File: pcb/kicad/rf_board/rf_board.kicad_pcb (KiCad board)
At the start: 2 copper layers, 89.5 x 70 mm, 14 parts, among them J1 B2B_A, J2 B2B_B, J3 UART_DBG, U1 CC1101_433_MODULE, U2 HC-05

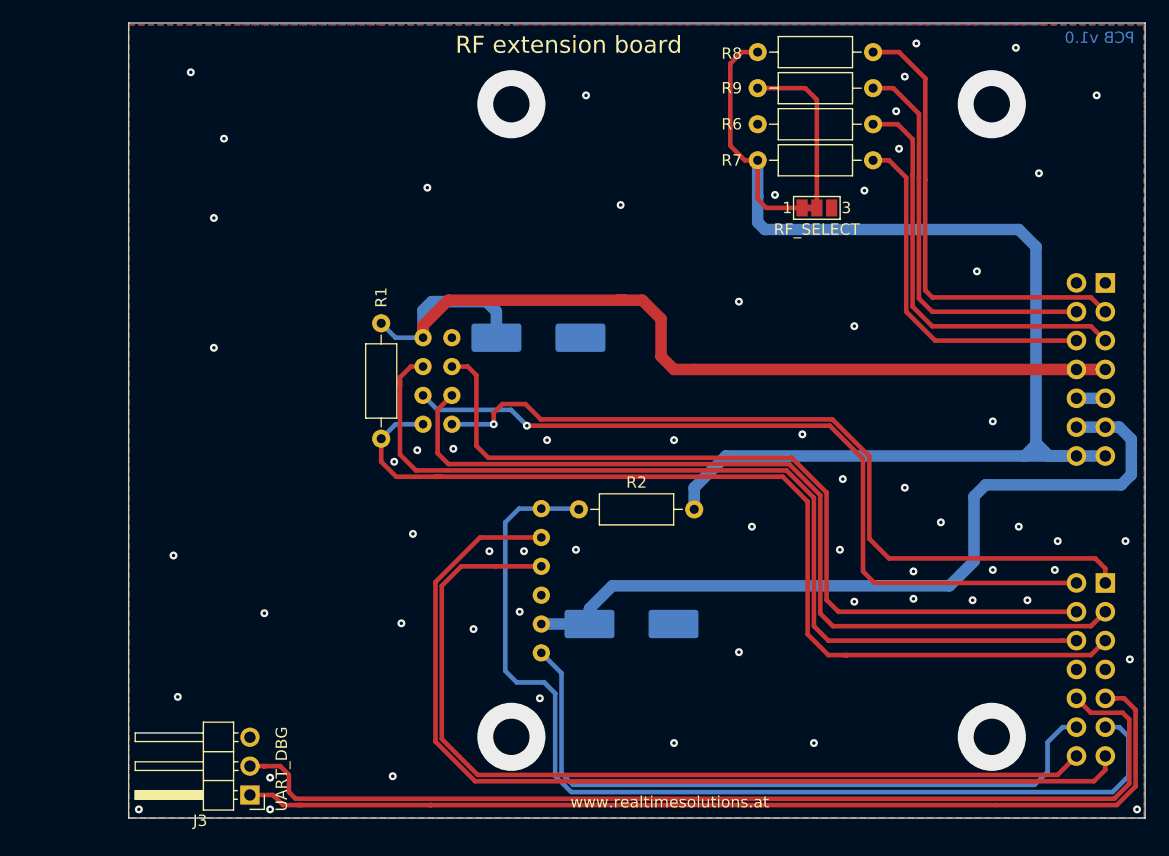
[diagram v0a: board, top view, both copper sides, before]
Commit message: Add RF board PCB ver.2.0
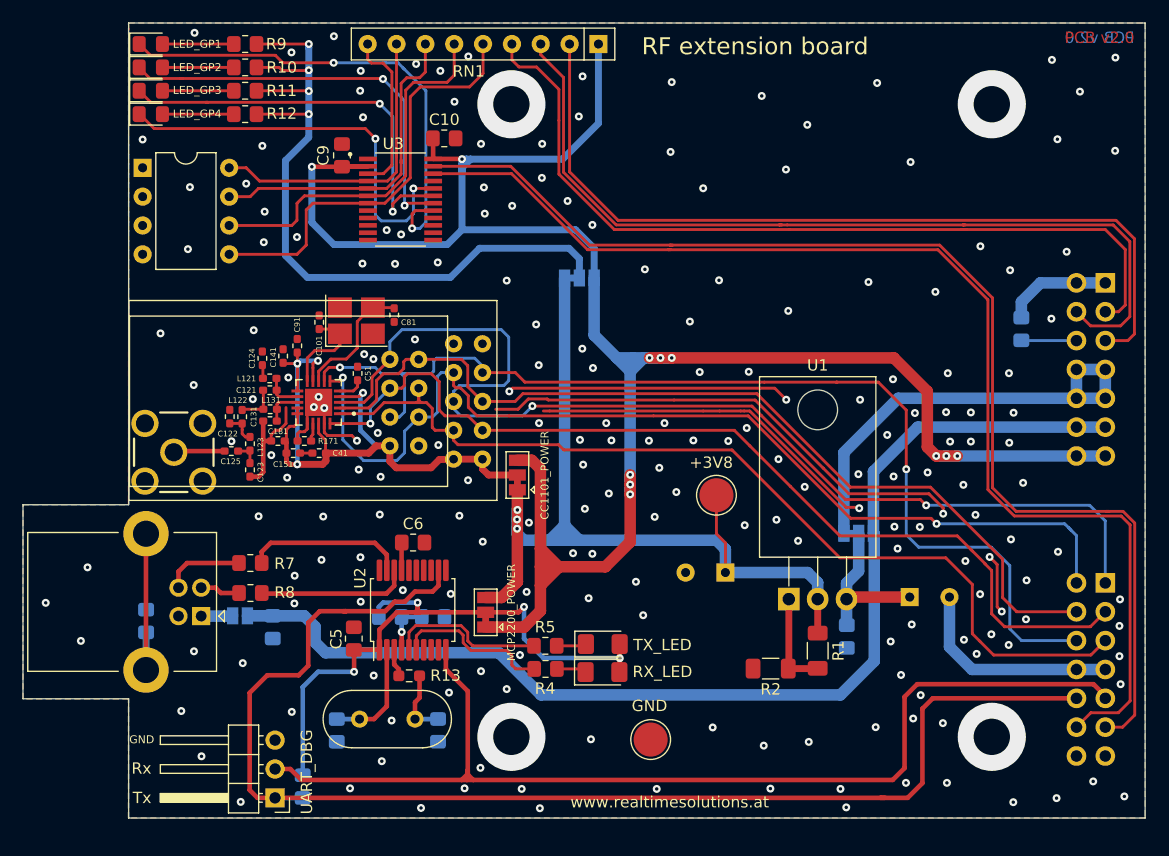
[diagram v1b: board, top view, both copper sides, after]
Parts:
- added C10: 100nF, Resistor_SMD:R_0805_2012Metric_Pad1.20x1.40mm_HandSolder, F.Cu at (12.8, -59.8)
- added C101: 27pF, Resistor_SMD:R_0402_1005Metric_Pad0.72x0.64mm_HandSolder, F.Cu at (1.78, -43.7)
- added C11: 10nF, Resistor_SMD:R_0805_2012Metric_Pad1.20x1.40mm_HandSolder, B.Cu at (-2.31, -16.8)
- added C121: 3.9pF, Resistor_SMD:R_0402_1005Metric_Pad0.72x0.64mm_HandSolder, F.Cu at (-2.57, -37.7)
- added C122: 8.2pF, Resistor_SMD:R_0402_1005Metric_Pad0.72x0.64mm_HandSolder, F.Cu at (-6.10, -35.3)
- added C123: 5.6pF, Resistor_SMD:R_0402_1005Metric_Pad0.72x0.64mm_HandSolder, F.Cu at (-4.32, -30.7)
- added C124: 220pF, Resistor_SMD:R_0402_1005Metric_Pad0.72x0.64mm_HandSolder, F.Cu at (-3.23, -40.5)
- added C125: 220pF, Resistor_SMD:R_0402_1005Metric_Pad0.72x0.64mm_HandSolder, F.Cu at (-5.96, -32.3)
- added C131: 3.9pF, Resistor_SMD:R_0402_1005Metric_Pad0.72x0.64mm_HandSolder, F.Cu at (-2.55, -35.0)
- added C141: 10nF, Resistor_SMD:R_0402_1005Metric_Pad0.72x0.64mm_HandSolder, F.Cu at (-1.40, -40.7)
- added C151: 220pF, Resistor_SMD:R_0402_1005Metric_Pad0.72x0.64mm_HandSolder, F.Cu at (-0.51, -32.1)
- added C181: 220pF, Resistor_SMD:R_0402_1005Metric_Pad0.72x0.64mm_HandSolder, F.Cu at (-1.85, -33.2)
- added C3: 220uF, Capacitor_THT:CP_Radial_D8.0mm_P3.50mm, B.Cu at (37.5, -21.6)
- added C4: 100nF, Resistor_SMD:R_0805_2012Metric_Pad1.20x1.40mm_HandSolder, B.Cu at (11.8, -17.7)
- added C41: 100nF, Resistor_SMD:R_0402_1005Metric_Pad0.72x0.64mm_HandSolder, F.Cu at (1.78, -32.1)
- added C5: 100nF, Resistor_SMD:R_0805_2012Metric_Pad1.20x1.40mm_HandSolder, F.Cu at (4.83, -15.8)
- added C51: 100nF, Resistor_SMD:R_0402_1005Metric_Pad0.72x0.64mm_HandSolder, F.Cu at (5.16, -39.1)
- added C6: 100nF, Resistor_SMD:R_0805_2012Metric_Pad1.20x1.40mm_HandSolder, F.Cu at (10.0, -24.3)
- added C7: 22pF, Resistor_SMD:R_0805_2012Metric_Pad1.20x1.40mm_HandSolder, B.Cu at (3.33, -7.71)
- added C8: 22pF, Resistor_SMD:R_0805_2012Metric_Pad1.20x1.40mm_HandSolder, B.Cu at (12.2, -7.72)
- added C81: 27pF, Resistor_SMD:R_0402_1005Metric_Pad0.72x0.64mm_HandSolder, F.Cu at (8.38, -44.3)
- added C9: 100nF, Resistor_SMD:R_0805_2012Metric_Pad1.20x1.40mm_HandSolder, F.Cu at (3.78, -58.3)
- added C91: 100nF, Resistor_SMD:R_0402_1005Metric_Pad0.72x0.64mm_HandSolder, F.Cu at (-0.15, -41.6)
- added D1: RX_LED, LED_SMD:LED_1206_3216Metric_Pad1.42x1.75mm_HandSolder, F.Cu at (26.7, -12.9)
- added D2: TX_LED, LED_SMD:LED_1206_3216Metric_Pad1.42x1.75mm_HandSolder, F.Cu at (26.7, -15.3)
- added D3: LED_GP1, LED_SMD:LED_0805_2012Metric_Pad1.15x1.40mm_HandSolder, F.Cu at (-13.0, -68.1)
- added D4: LED_GP2, LED_SMD:LED_0805_2012Metric_Pad1.15x1.40mm_HandSolder, F.Cu at (-13.0, -66.1)
- added D5: LED_GP3, LED_SMD:LED_0805_2012Metric_Pad1.15x1.40mm_HandSolder, F.Cu at (-13.0, -64.0)
- added D6: LED_GP4, LED_SMD:LED_0805_2012Metric_Pad1.15x1.40mm_HandSolder, F.Cu at (-13.0, -62.0)
- added J4: USB_B, Connector_USB:USB_B_Lumberg_2411_02_Horizontal, F.Cu at (-8.61, -17.8)
- added J5: Antenna 50 Ohm, SMA-J-P-X-ST-TH1:SAMTEC_SMA-J-P-X-ST-TH1, F.Cu at (-11.0, -32.2)
- added JP2: Vusb, Jumper:SolderJumper-2_P1.3mm_Open_Pad1.0x1.5mm, B.Cu at (-5.19, -17.8)
- added JP3: LM317_POWER, Jumper:SolderJumper-3_P1.3mm_Bridged12_Pad1.0x1.5mm, B.Cu at (49.3, -25.1)
- added JP4: CC1101_POWER, Jumper:SolderJumper-3_P1.3mm_Bridged12_Pad1.0x1.5mm, F.Cu at (19.2, -30.2)
- added JP5: LED_POWER, Jumper:SolderJumper-3_P1.3mm_Bridged12_Pad1.0x1.5mm, B.Cu at (24.7, -47.5)
- added L121: 27nH, Resistor_SMD:R_0402_1005Metric_Pad0.72x0.64mm_HandSolder, F.Cu at (-2.58, -38.7)
- added L122: 22nH, Resistor_SMD:R_0402_1005Metric_Pad0.72x0.64mm_HandSolder, F.Cu at (-5.00, -35.3)
- added L123: 27nH, Resistor_SMD:R_0402_1005Metric_Pad0.72x0.64mm_HandSolder, F.Cu at (-4.32, -33.0)
- added L131: 27nH, Resistor_SMD:R_0402_1005Metric_Pad0.72x0.64mm_HandSolder, F.Cu at (-2.54, -36.0)
- added R10: 220R, Resistor_SMD:R_0805_2012Metric_Pad1.20x1.40mm_HandSolder, F.Cu at (-4.74, -66.1)
- added R11: 220R, Resistor_SMD:R_0805_2012Metric_Pad1.20x1.40mm_HandSolder, F.Cu at (-4.74, -64.0)
- added R12: 220R, Resistor_SMD:R_0805_2012Metric_Pad1.20x1.40mm_HandSolder, F.Cu at (-4.74, -62.0)
- added R13: 0R, Resistor_SMD:R_0603_1608Metric_Pad0.98x0.95mm_HandSolder, F.Cu at (9.70, -12.5)
- added R14: 10K, Resistor_SMD:R_0805_2012Metric_Pad1.20x1.40mm_HandSolder, B.Cu at (63.6, -43.1)
- added R171: 56K, Resistor_SMD:R_0402_1005Metric_Pad0.72x0.64mm_HandSolder, F.Cu at (0.47, -33.2)
- added R3: 33K, Resistor_SMD:R_0805_2012Metric_Pad1.20x1.40mm_HandSolder, B.Cu at (0.33, -2.77)
- added R4: 2K2, Resistor_SMD:R_0805_2012Metric_Pad1.20x1.40mm_HandSolder, F.Cu at (21.7, -13.1)
- added R5: 2K2, Resistor_SMD:R_0805_2012Metric_Pad1.20x1.40mm_HandSolder, F.Cu at (21.7, -15.2)
- added RN1: R_Network08, Resistor_THT:R_Array_SIP9, F.Cu at (26.4, -68.1)
- added RV1: Varistor, Resistor_SMD:R_0805_2012Metric_Pad1.20x1.40mm_HandSolder, B.Cu at (-13.5, -17.3)
- added SW1: SW_DIP_x04, Package_DIP:DIP-8_W7.62mm, F.Cu at (-13.8, -57.3)
- added TP1: +3V8, TestPoint:TestPoint_Pad_D3.0mm, F.Cu at (36.8, -28.4)
- added TP2: GND, TestPoint:TestPoint_Pad_D3.0mm, F.Cu at (31.0, -6.91)
- added U3: TCA6416APWR, TCA6416APWR:SOP65P640X120-24N, F.Cu at (8.94, -54.5)
- added U4: CC1101_433_MODULE, cc1101:CC1101_MODULE, F.Cu at (17.4, -45.6)
- added U5: CC1101_433_MODULE_SMALL, cc1101:CC1101_MODULE_SMALL, F.Cu at (13.1, -44.2)
- added U6: CC1101RGPR, CC1101RGPR:QFN50P400X400X100-21N, F.Cu at (1.73, -36.6)
- added XTAL1: 26Mhz, Crystal:Crystal_SMD_3225-4Pin_3.2x2.5mm_HandSoldering, F.Cu at (5.05, -43.8)
- added XTAL2: 12MHz, Crystal:Crystal_HC49-U_Vertical, F.Cu at (5.33, -8.71)
- C1: value 100uF/25V -> 100uF; footprint Capacitor_SMD:CP_Elec_8x10.5 -> Capacitor_THT:CP_Radial_D8.0mm_P3.50mm
- C2: value 100uF/25V -> 100nF; footprint Capacitor_SMD:CP_Elec_8x10.5 -> Resistor_SMD:R_0805_2012Metric_Pad1.20x1.40mm_HandSolder
- JP1: value RF_SELECT -> MCP2200_POWER; footprint Jumper:SolderJumper-3_P1.3mm_Bridged12_Pad1.0x1.5mm_NumberLabels -> Jumper:SolderJumper-3_P1.3mm_Bridged12_Pad1.0x1.5mm
- R1: value 10K -> 1K2; footprint Resistor_THT:R_Axial_DIN0207_L6.3mm_D2.5mm_P10.16mm_Horizontal -> Resistor_SMD:R_1206_3216Metric_Pad1.30x1.75mm_HandSolder
- R2: value 10K -> 2K; footprint Resistor_THT:R_Axial_DIN0207_L6.3mm_D2.5mm_P10.16mm_Horizontal -> Resistor_SMD:R_1206_3216Metric_Pad1.30x1.75mm_HandSolder
- R6: footprint Resistor_THT:R_Axial_DIN0207_L6.3mm_D2.5mm_P10.16mm_Horizontal -> Resistor_SMD:R_0805_2012Metric_Pad1.20x1.40mm_HandSolder; moved to B.Cu
- R7, R8: value 10K -> 22R; footprint Resistor_THT:R_Axial_DIN0207_L6.3mm_D2.5mm_P10.16mm_Horizontal -> Resistor_SMD:R_0805_2012Metric_Pad1.20x1.40mm_HandSolder
- R9: value 10K -> 220R; footprint Resistor_THT:R_Axial_DIN0207_L6.3mm_D2.5mm_P10.16mm_Horizontal -> Resistor_SMD:R_0805_2012Metric_Pad1.20x1.40mm_HandSolder
- U1: value CC1101_433_MODULE -> LM317_TO-220; footprint cc1101:CC1101_MODULE -> Package_TO_SOT_THT:TO-220-3_Horizontal_TabDown; moved to F.Cu
- U2: value HC-05 -> MCP2200-I-SS; footprint bluetooth:HC-05_MODULE -> Package_SO:SSOP-20_5.3x7.2mm_P0.65mm; moved to F.Cu
- moved R8 65.3 mm to (-4.28, -19.8)
- moved R7 57.0 mm to (-4.28, -22.5)
- moved R6 54.1 mm to (8.03, -17.7)
- moved R1 48.0 mm to (45.7, -14.7)
- moved JP1 46.0 mm to (16.4, -18.1), turned to 90 degrees
- moved R9 45.3 mm to (-4.74, -68.1)
- moved C1 39.9 mm to (53.8, -19.5)
- moved U1 30.7 mm to (43.1, -19.3), turned to 0 degrees
- moved R2 22.0 mm to (41.5, -13.2), turned to 180 degrees
- moved C2 19.0 mm to (48.2, -16.0), turned to 270 degrees
- moved U2 13.7 mm to (10.0, -18.3), turned to 90 degrees
- moved J3 2.22 mm to (-2.11, -1.78)
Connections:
- C1 pad 1: +4V -> Net-(C1-Pad1)
- C2 pad 1: +5V -> Net-(C1-Pad1)
- J1 pad 3: HW_ADDR3 -> HW_ADDR4
- J1 pad 4: HW_ADDR4 -> HW_ADDR3
- J1 pad 5: HW_ADDR1 -> HW_ADDR2
- J1 pad 6: HW_ADDR2 -> HW_ADDR1
- J1 pad 7: +4V -> +12V
- J1 pad 8: +4V -> +12V
- J2 pad 1: IO1 -> IO2
- J2 pad 10: UART2_RX -> UART2_TX
- J2 pad 11: IO3 -> I2C_SDA
- J2 pad 12: IO4 -> I2C_SCK
- J2 pad 13: UART1_TX -> UART1_RX
- J2 pad 14: UART1_RX -> UART1_TX
- J2 pad 2: IO2 -> IO1
- J2 pad 3: SPI_MISO -> SPI_MOSI
- J2 pad 4: SPI_MOSI -> SPI_MISO
- J2 pad 5: SPI_CS -> SPI_CLK
- J2 pad 6: SPI_CLK -> SPI_CS
- J2 pad 9: UART2_TX -> UART2_RX
- JP1 pad 2: Net-(JP1-Pad2) -> Net-(C5-Pad2)
- JP1 pad 3: GND -> +3V8
- R1 pad 1: +4V -> +3V8
- R1 pad 2: SPI_CS -> Net-(R1-Pad2)
- R2 pad 1: IO3 -> Net-(R1-Pad2)
- R2 pad 2: +3V3 -> GND
- R6 pad 1: GND -> Net-(C5-Pad2)
- R6 pad 2: HW_ADDR1 -> Net-(C4-Pad2)
- R7 pad 1: +3V3 -> Net-(J4-Pad3)
- R7 pad 2: HW_ADDR2 -> Net-(R7-Pad2)
- R8 pad 1: +3V3 -> Net-(J4-Pad2)
- R8 pad 2: HW_ADDR3 -> Net-(R8-Pad2)
- R9 pad 1: Net-(JP1-Pad2) -> Net-(D3-Pad2)
- R9 pad 2: HW_ADDR4 -> Net-(JP5-Pad2)
- U1 pad 1: GND -> Net-(R1-Pad2)
- U1 pad 2: +4V -> +3V8
- U1 pad 3: SPI_MOSI -> Net-(C1-Pad1)
- U2 pad 1: IO3 -> Net-(C5-Pad2)
- U2 pad 2: UART1_TX -> Net-(C7-Pad2)
- U2 pad 3: UART1_RX -> Net-(R13-Pad2)
- U2 pad 4: GND -> Net-(C4-Pad2)
- U2 pad 5: +5V -> Net-(R5-Pad2)
- U2 pad 6: IO4 -> Net-(R4-Pad2)
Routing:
- net GND: track 0.00 -> 155.9 mm, vias 61 -> 206
- net I2C_SCK: track 0.00 -> 105.3 mm
- net I2C_SDA: track 0.00 -> 104.9 mm
- net +3V8: track 0.00 -> 91.7 mm, vias 0 -> 3
- net IO3: track 90.1 -> 0.00 mm
- net UART1_TX: track 87.1 -> 0.00 mm
- net +4V: track 83.2 -> 0.00 mm
- net UART1_RX: track 80.8 -> 0.00 mm
- net +3V3: track 113.6 -> 191.2 mm, vias 0 -> 11
- net Net-(JP5-Pad2): track 0.00 -> 67.8 mm, vias 0 -> 4
- net Net-(C141-Pad2): track 0.00 -> 64.2 mm, vias 0 -> 4
- net IO4: track 60.7 -> 0.00 mm
- net Net-(C5-Pad2): track 0.00 -> 58.5 mm, vias 0 -> 4
- net Net-(D3-Pad1): track 0.00 -> 43.7 mm, vias 0 -> 2
- net HW_ADDR2: track 31.4 -> 74.6 mm
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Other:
- board size 89.5 x 70 mm -> 98.8 x 70 mm
- board text added: "GND"
- board text added: "PCB v2.0"
- board text added: "Rx"
- board text added: "Tx"
- board text removed: "PCB v1.0"
